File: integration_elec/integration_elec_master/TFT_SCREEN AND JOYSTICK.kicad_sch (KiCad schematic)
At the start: 2 parts, among them U5 COM-28379, U6 COM-09032

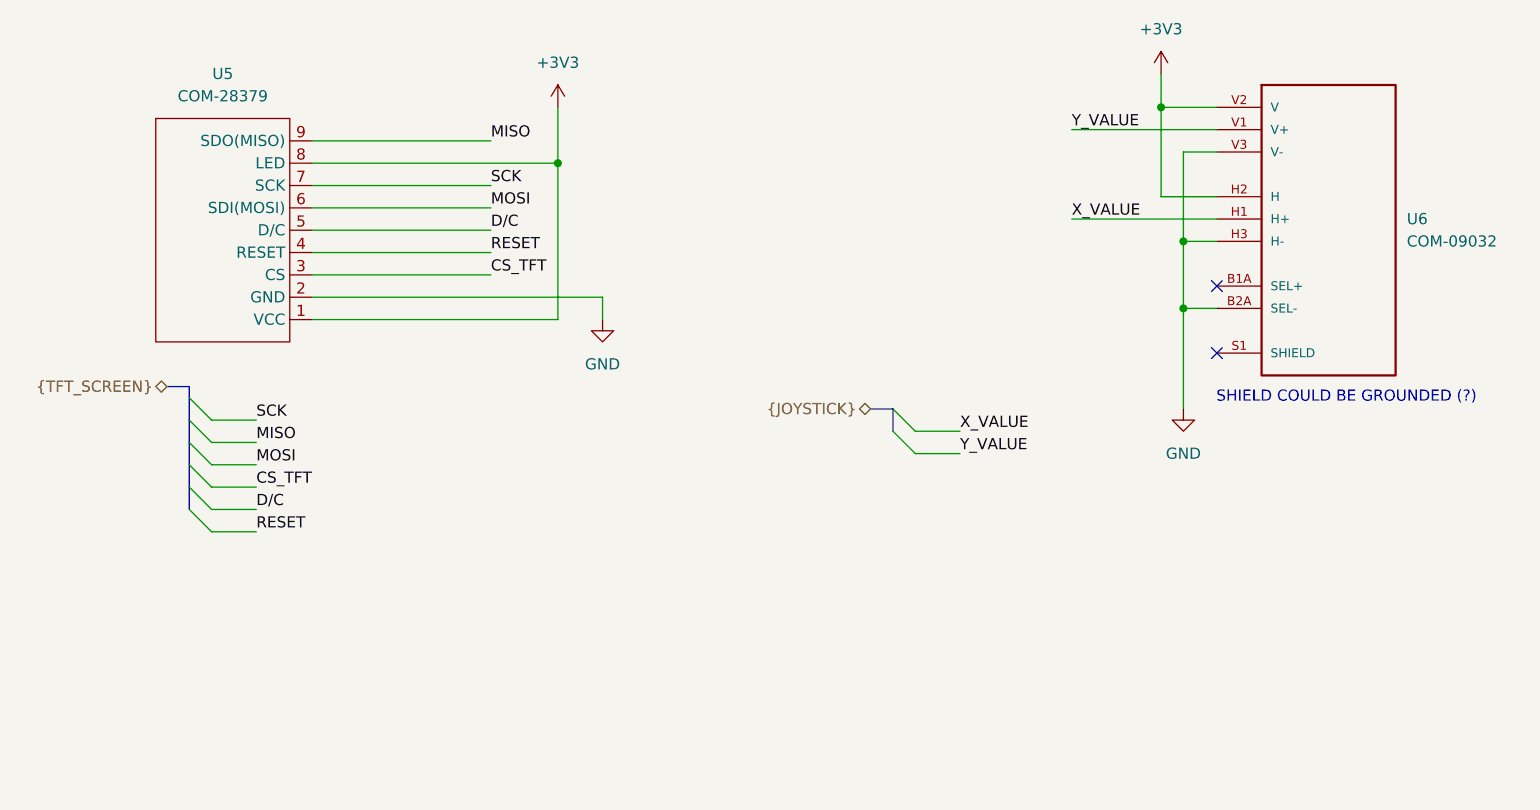
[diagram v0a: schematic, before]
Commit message: Added plein de footprint
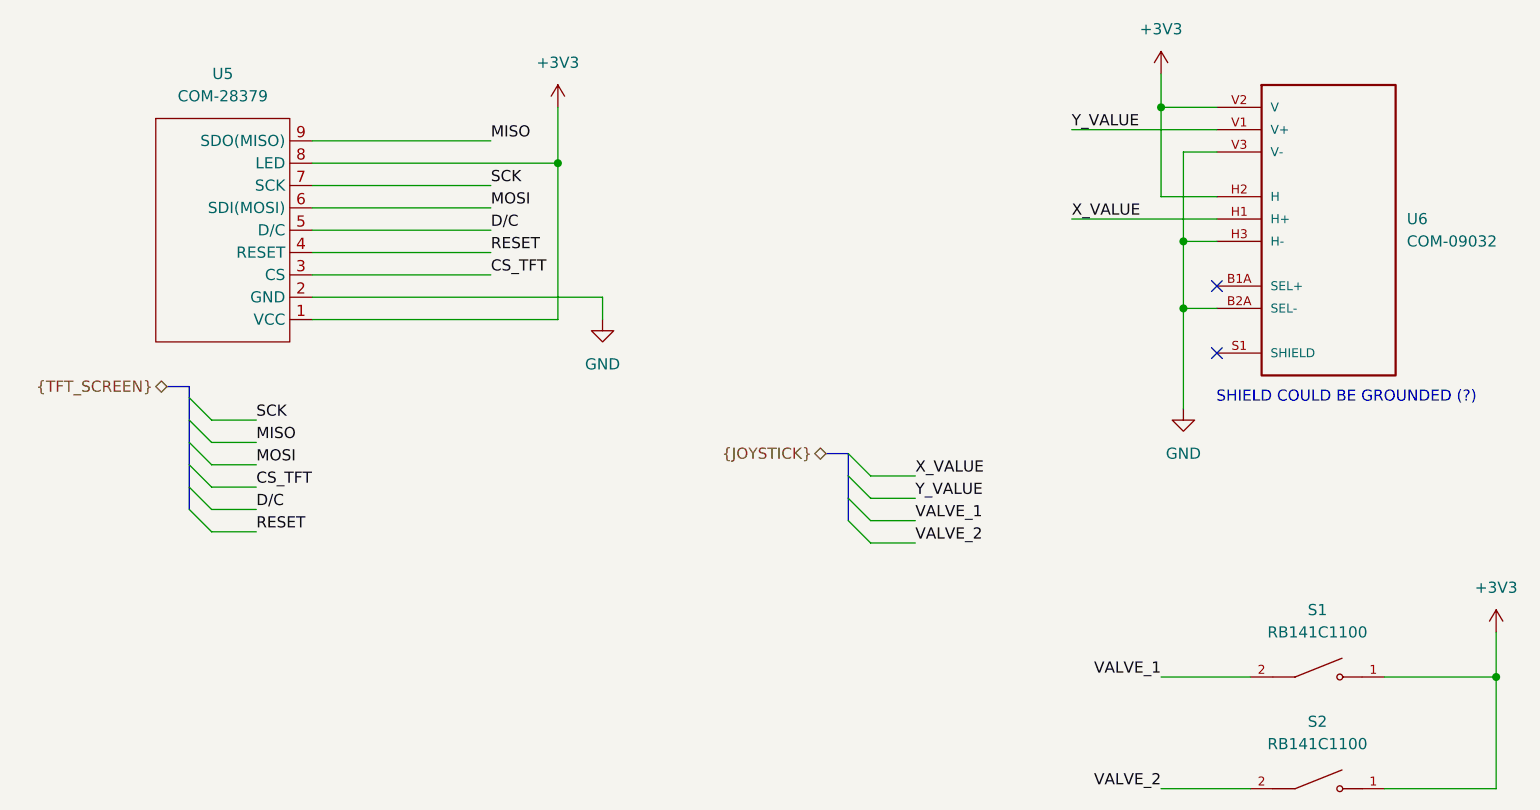
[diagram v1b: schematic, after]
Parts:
- added S1, S2: RB141C1100, JOYSTICK:SWITCH, symbol RB141C1100:RB141C1100
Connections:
- net +3V3: now also S1.1, S2.1
- new net VALVE_1: S1.2
- new net VALVE_2: S2.2

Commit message: Added comment for pull-down
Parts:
- S1, S2: Digikey (none) -> EG5637-ND
- U6: Digikey (none) -> 1568-09032-ND
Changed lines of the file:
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@@
+			)
+		)
+		(property "Digikey" "1568-09032-ND"
+			(at 171.45 49.53 0)
+			(effects
+				(font
+					(size 1.27 1.27)
+				)
+				(hide yes)
 			)
 		)
@@
 			)
 		)
+		(property "Digikey" "EG5637-ND"
+			(at 170.18 101.6 0)
+			(effects
+				(font
+					(size 1.27 1.27)
+				)
+				(hide yes)
+			)
+		)
 		(pin "2"
 		)
@@
 				(hide yes)
 			)
+		)
+		(property "Digikey" "EG5637-ND"
+			(at 170.18 114.3 0)
+			(effects
+				(font
+					(size 1.27 1.27)
+				)
+				(hide yes)
+			)

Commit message: KAH - Fini schematic attente de review + correction BUS
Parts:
- removed U6: COM-09032, JOYSTICK:XDCR_COM-09032, symbol COM-09032:COM-09032
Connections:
- net RESET renamed RESET_TFT
- no-connect marks 2 -> 0
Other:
- note removed: "SHIELD COULD BE GROUNDED (?)"

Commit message: KAH - layout continué, un imbecile a mis le 3v3 tout en bas a droite tres loin de tout
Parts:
- S1, S2: DigiKey (none) -> EG5637-ND
- U5: DigiKey (none) -> 1568-COM-28379-ND
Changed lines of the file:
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@@
+			)
+		)
+		(property "DigiKey" "1568-COM-28379-ND"
+			(at 38.1 38.1 0)
+			(effects
+				(font
+					(size 1.27 1.27)
+				)
+				(hide yes)
 			)
 		)
@@
 			)
 		)
+		(property "DigiKey" "EG5637-ND"
+			(at 170.18 101.6 0)
+			(effects
+				(font
+					(size 1.27 1.27)
+				)
+				(hide yes)
+			)
+		)
 		(pin "2"
 		)
@@
 			(at 170.18 114.3 0)
 			(effects
+				(font
+					(size 1.27 1.27)
+				)
+				(hide yes)
+			)
+		)
+		(property "DigiKey" "EG5637-ND"
+			(at 170.18 114.3 0)
+			(effects
